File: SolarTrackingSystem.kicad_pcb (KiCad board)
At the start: 2 copper layers, 57 x 55 mm, 15 parts, among them J1 Servo Pin Connector, J2 LDR Terminal, J3 LDR Terminal (1), U1 DS1302+, Y1 Crystal

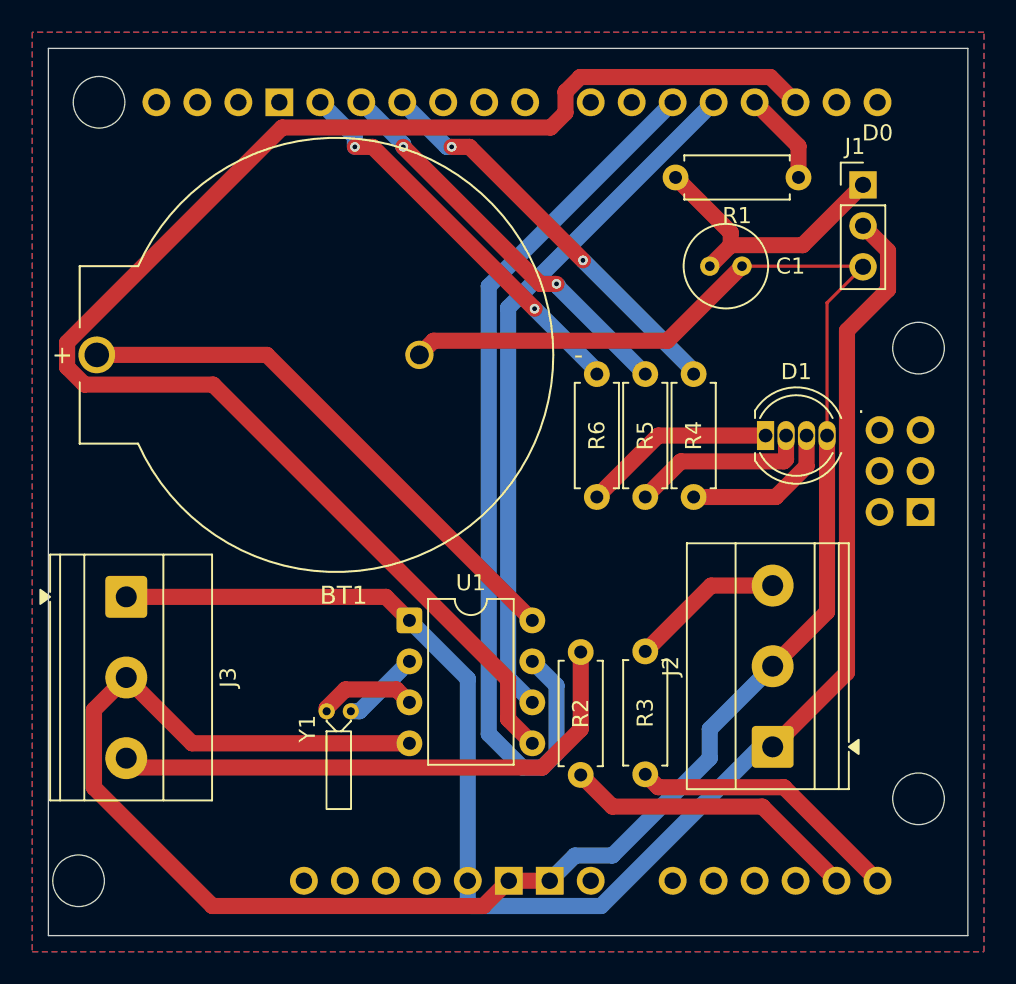
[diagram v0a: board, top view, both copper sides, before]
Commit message: changed from double-sided to  single-sided
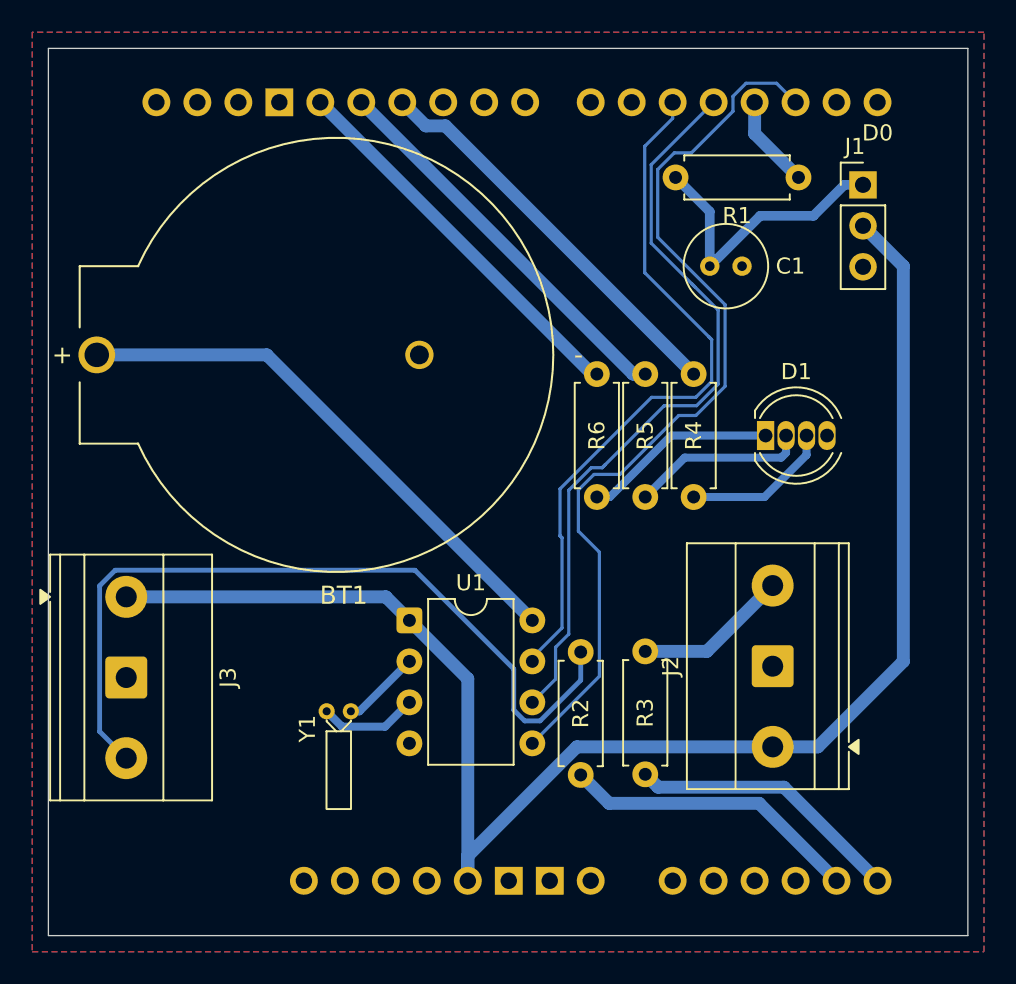
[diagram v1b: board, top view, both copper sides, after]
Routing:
- net GND: track 136.2 -> 0.00 mm
- net /RTC_RST: track 94.8 -> 56.7 mm
- net Net-(J3-Pin_3): track 34.2 -> 49.7 mm
- net /RTC_CLK: track 55.6 -> 43.8 mm
- net /RTC_DATA: track 43.1 -> 47.3 mm
- net /5V_pin: track 96.2 -> 97.7 mm
- net Net-(J1-Pin_1): track 17.2 -> 18.0 mm
- net Net-(A1-PadD13): track 24.6 -> 24.1 mm, vias 2 -> 0
- net Net-(A1-PadD12): track 24.8 -> 24.6 mm, vias 2 -> 0
- net Net-(A1-PadD11): track 25.2 -> 25.0 mm, vias 2 -> 0
